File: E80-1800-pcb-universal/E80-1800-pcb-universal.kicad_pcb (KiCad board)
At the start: 2 copper layers, 382 x 160 mm, 329 parts, among them J1 SPI, J2 OLED, J3 USB_C_Receptacle_USB2.0, J4 BATT, Q1 AO3400A, SW1 RST, SW2 BOOT, U1 SRV05-4, U2 XC6206P332MR, U3 STM32F072RBTx

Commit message: added logo
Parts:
- added G***: LOGO, logo-branding:logo_mask_20, B.Cu at (218.5, 18.8)

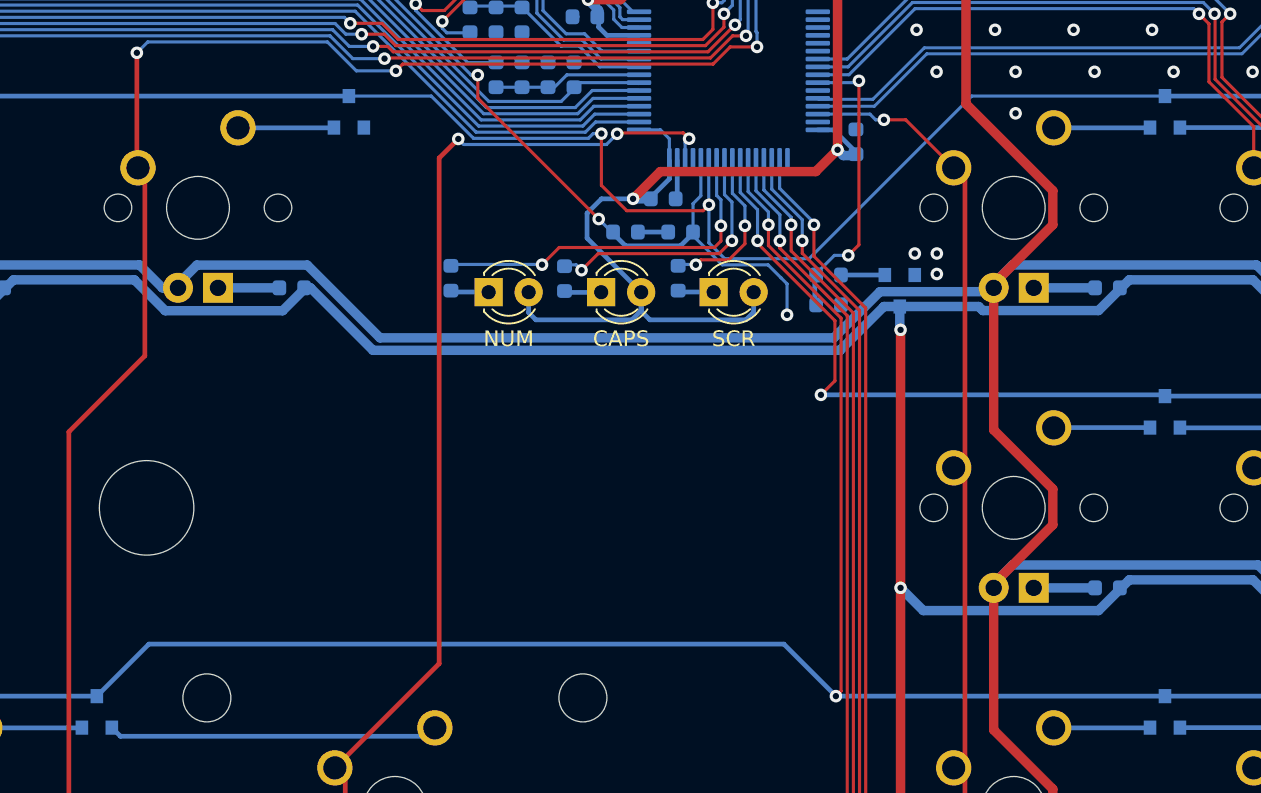
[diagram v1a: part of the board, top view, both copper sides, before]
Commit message: minor routing improvements, added missing cap
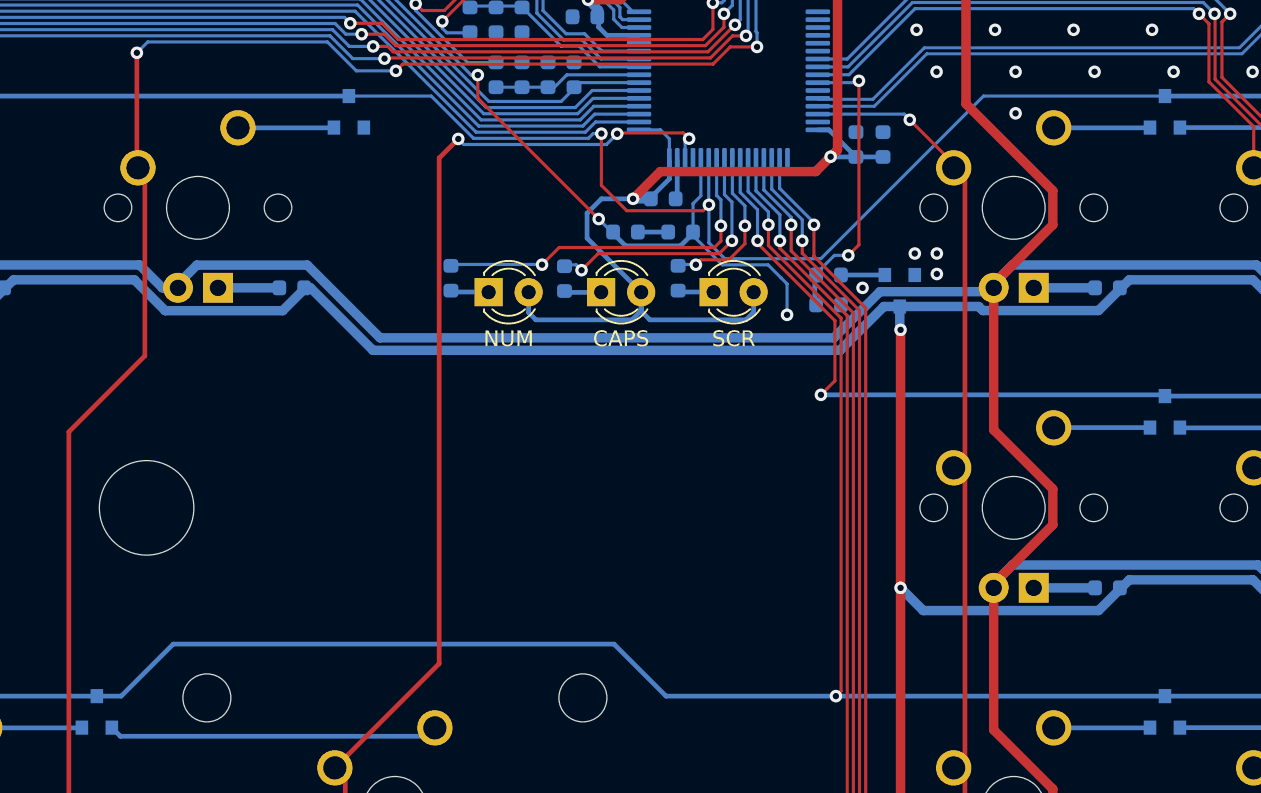
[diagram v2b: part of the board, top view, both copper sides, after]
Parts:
- removed the G*** at (218.5, 18.8)
- added C7: 4.7uF, kicad-keyboard-parts:C_0603_1608Metric_stealth, B.Cu at (288.2, -4.02)
- added G***: LOGO, logo-branding:logo_mask_15, B.Cu at (224.9, 19.0)
- moved C8 0.17 mm to (286.4, -4.02)
- renumbered C11 to C10, C10 to C11, C9 to C12, C8 to C13, C13 to C14, C14 to C15, C15 to C16, C16 to C17, C12 to C6, C6 to C8, C7 to C9, J4 to J2, J2 to J3, J3 to J4, R7 to R10, R8 to R7, R9 to R8, R10 to R9
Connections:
- J1 pad MP: GND -> (no net)
- J2 pad MP: GND -> (no net)
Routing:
- net +3V3: track 487.3 -> 489.2 mm
- net GND: vias 109 -> 110

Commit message: moved 4u7 to a better spot
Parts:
- removed the C6 at (274.3, -19.6)
- removed G***: LOGO, logo-branding:logo_mask_15
- renumbered C11 to C10, C12 to C11, C13 to C12, C14 to C13, C15 to C14, C16 to C15, C17 to C16, C7 to C6, C8 to C7, C9 to C8, C10 to C9
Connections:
- D10 pad 1: Net-(D10-Pad1) -> (no net)
- D57 pad 1: Net-(D57-Pad1) -> (no net)
- J4 pad A8: Net-(J4-PadA8) -> (no net)
- J4 pad B8: Net-(J4-PadB8) -> (no net)
- U3 pad 33: Net-(U3-Pad33) -> (no net)
- U3 pad 34: Net-(U3-Pad34) -> (no net)
- U3 pad 35: Net-(U3-Pad35) -> (no net)
- U3 pad 36: Net-(U3-Pad36) -> (no net)
- U3 pad 37: Net-(U3-Pad37) -> (no net)
- U3 pad 38: Net-(U3-Pad38) -> (no net)
- U3 pad 43: Net-(U3-Pad43) -> (no net)
- U3 pad 49: Net-(U3-Pad49) -> (no net)
- U3 pad 61: Net-(U3-Pad61) -> (no net)

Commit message: re-added logo
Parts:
- added G***: LOGO, logo-branding:logo_mask_15, B.Cu at (224.7, 19.0)
